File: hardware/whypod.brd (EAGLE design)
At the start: 100 x 80 mm, 13 parts, among them IC1 IC_USBLC6-2, X2 USB-A-S, Y1 CRYSTAL-GROUNDEDSMD-5X3.2

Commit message: Hardware updates
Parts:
- removed R3: 0R, rcl:R0603
- added C6, C7, C8, C9: (no value), rcl:C0603
- moved C4 2.80 mm to (56.1, 46.9)
- moved C1 2.54 mm to (25.4, 39.8)
- moved C2 2.54 mm to (25.4, 41.9)
- moved C3 2.54 mm to (51.0, 28.6)
- moved C5 2.54 mm to (51.5, 30.6)
- moved IC1 2.54 mm to (80.6, 44.4)
- moved R5 2.54 mm to (58.7, 36.7)
- moved U$2 2.54 mm to (44.2, 40.6)
- moved X2 2.54 mm to (89.3, 44.4)
- moved Y1 2.54 mm to (30.2, 40.9)
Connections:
- removed net N$5: R3.1, U$2.PD7
- new net LCD_BACKLIGHT: U$2.PC6
- new net SDIO_CLK: U$2.PC12
- new net SDIO_CMD: U$2.PD2
- new net SDIO_D0: U$2.PC8
- new net SDIO_D1: U$2.PC9
- new net SDIO_D2: U$2.PC10
- new net SDIO_D3: U$2.PC11
- net 3V: now also C6.1, C7.1, C8.1, C9.1
- net GND: now also C6.2, C7.2, C8.2, C9.2
- net LCD_CS: now also U$2.PD7; no longer R3.2
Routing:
- net 3V: track 2.42 -> 56.9 mm
- net DB2: track 4.29 -> 52.5 mm
- net SDIO_D1: track 0.00 -> 36.2 mm, vias 0 -> 1
- net SDIO_D0: track 0.00 -> 35.0 mm, vias 0 -> 1
- net LCD_BACKLIGHT: track 0.00 -> 34.4 mm
- net LCD_RD: track 15.2 -> 41.5 mm
- net LCD_WR: track 13.4 -> 39.4 mm
- net GND: track 0.00 -> 14.0 mm, vias 5 -> 8
- net LCD_CS: track 39.1 -> 49.4 mm
- net DB3: track 53.8 -> 45.9 mm
- net N$7: track 0.00 -> 4.28 mm
- net DB1: track 100.5 -> 97.9 mm
- net SD_CLK: track 64.8 -> 62.2 mm
- net T_CLK: track 46.7 -> 44.2 mm
- net SD_DO: track 62.7 -> 60.2 mm
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
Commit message: Hardware updated
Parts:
- added C10: (no value), rcl:C0603
- added JP1: (no value), pinhead-2:1X04SMD/90
- added R1, R2: 0R, rcl:R0603
- added R10, R11, R3, R6, R8: (no value), rcl:R0603
- added R7, R9: (no value), rcl:R0402
- added U1: USD-SOCKETUSD, SparkFun-Connectors:USD-SOCKET-PP
- moved IC1 27.9 mm to (52.7, 44.4)
- moved X2 27.9 mm to (61.4, 44.4)
- moved C3 14.6 mm to (36.4, 28.6)
- moved C4 14.6 mm to (41.5, 46.9)
- moved C8 14.6 mm to (22.4, 50.2)
- moved C9 14.6 mm to (38.9, 47.9)
- moved C6 14.6 mm to (23.4, 30.6)
- moved C7 14.6 mm to (19.1, 42.9)
- moved JP2 14.6 mm to (14.6, 15.2)
- moved U$2 14.6 mm to (29.6, 40.6)
- moved C1 14.6 mm to (10.8, 39.8)
- moved C2 14.6 mm to (10.8, 41.9)
- moved Y1 14.6 mm to (15.6, 40.9)
- moved C5 14.6 mm to (36.9, 30.6)
- moved R4 14.6 mm to (37.2, 20.7)
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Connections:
- new net N$5: R1.2, U$2.PC10
- new net N$8: R2.2, U$2.PC11
- new net SDIO_CD: R10.1, U$2.PD3, U1.CD1
- net 3V: now also C10.1, R10.2, R11.2, R3.2, R6.2, R7.2, R8.2, R9.2, U1.4
- net GND: now also C10.2, U1.6, U1.CD2, U1.GND1, U1.GND2
- net SDIO_CLK: now also R9.1, U1.5
- net SDIO_CMD: now also R11.1, U1.3
- net SDIO_D0: now also R3.1, U1.7
- net SDIO_D1: now also R6.1, U1.8
- net SDIO_D2: now also R1.1, R7.1, U1.1; no longer U$2.PC10
- net SDIO_D3: now also R2.1, R8.1, U1.2; no longer U$2.PC11
- net SWD_CLK: now also JP1.4
- net SWD_IO: now also JP1.3
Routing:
- net SDIO_CD: track 0.00 -> 42.5 mm
- net SWD_IO: track 0.00 -> 38.5 mm
- net 3V: track 56.9 -> 92.2 mm, vias 0 -> 3
- net SDIO_CMD: track 0.00 -> 31.6 mm
- net SWD_CLK: track 0.00 -> 28.6 mm
- net SDIO_D1: track 36.2 -> 64.5 mm, vias 1 -> 2
- net SDIO_D0: track 35.0 -> 63.1 mm, vias 1 -> 2
- net LCD_CS: track 49.4 -> 76.9 mm, vias 1 -> 2
- net SDIO_CLK: track 0.00 -> 26.6 mm
- net LCD_WR: track 39.4 -> 62.9 mm, vias 1 -> 2
- net N$5: track 0.00 -> 21.2 mm
- net N$8: track 0.00 -> 18.1 mm
- net SDIO_D3: track 0.00 -> 15.1 mm
- net DB3: track 45.9 -> 60.4 mm, vias 3 -> 2
- net LCD_RD: track 41.5 -> 55.3 mm
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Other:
- board size 100 x 80 mm -> 72.1 x 85.1 mm

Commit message: PCB updates
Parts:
- removed JP1: (no value), pinhead-2:1X04SMD/90
- added J1: AUDIO_JACK_TRRSSMD_RA, SparkFun-Connectors:AUDIO_JACK_3.5MM_TRRS_SMD_RA
- added JP3: (no value), pinhead-2:1X06SMD/90
- added U$1: WM8731, microdecv1:28-SSOP
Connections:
- new net AGND: U$1.P$15
- new net AVDD: U$1.P$14
- new net DBVDD: U$1.P$1
- new net DCVDD: U$1.P$27
- new net DGND: U$1.P$28
- new net HPGND: U$1.P$11
- new net HPVDD: U$1.P$8
- new net NRST: JP3.5, U$2.NRST
- new net SWD_SWO: JP3.6
- net 3V: now also JP3.1
- net GND: now also JP3.3
- net SWD_CLK: now also JP3.2; no longer JP1.4
- net SWD_IO: now also JP3.4; no longer JP1.3
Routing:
- net SWD_CLK: track 28.6 -> 7.10 mm
- net SWD_IO: track 38.5 -> 31.0 mm
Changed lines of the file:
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@@
 <element name="R10" library="rcl" package="R0603" value="" x="34.1685875" y="64.2112"/>
 <element name="R11" library="rcl" package="R0603" value="" x="35.867340625" y="66.1924" rot="R180"/>
-<element name="JP1" library="pinhead-2" package="1X04SMD/90" value="" x="64.77" y="62.865" rot="R270"/>
+<element name="JP3" library="pinhead-2" package="1X06SMD/90" value="" x="63.5" y="68.58" rot="R270"/>
+<element name="J1" library="SparkFun-Connectors" package="AUDIO_JACK_3.5MM_TRRS_SMD_RA" value="AUDIO_JACK_TRRSSMD_RA" x="19.05" y="83.82" rot="R270">
+<attribute name="PROD_ID" value="CONN-10676" x="19.05" y="83.82" size="1.778" layer="27" rot="R270" display="off"/>
+<attribute name="SF_ID" value="PRT-12639" x="19.05" y="83.82" size="1.778" layer="27" rot="R270" display="off"/>
+</element>
+<element name="U$1" library="microdecv1" package="28-SSOP" value="WM8731" x="19.05" y="63.5" rot="R270"/>
 </elements>
 <signals>
@@
 <via x="44.6786" y="66.3956" extent="1-16" drill="0.6" diameter="1.4224" shape="octagon"/>
 <wire x1="21.8918" y1="37.1146" x2="20.32" y2="37.1146" width="0.3048" layer="1"/>
+<contactref element="JP3" pad="3"/>
 </signal>
 <signal name="DB0">
@@
 <signal name="SWD_IO">
 <contactref element="U$2" pad="PA13"/>
-<contactref element="JP1" pad="3"/>
 <wire x1="37.3918" y1="45.1146" x2="42.3714" y2="45.1146" width="0.3048" layer="1"/>
 <wire x1="42.3714" y1="45.1146" x2="43.1038" y2="45.847" width="0.3048" layer="1"/>
-<wire x1="43.1038" y1="45.847" x2="43.1038" y2="54.5084" width="0.3048" layer="1"/>
-<wire x1="43.1038" y1="54.5084" x2="44.1452" y2="55.5498" width="0.3048" layer="1"/>
-<wire x1="61.0362" y1="55.5498" x2="44.1452" y2="55.5498" width="0.3048" layer="1"/>
-<wire x1="59.69" y1="59.055" x2="61.087" y2="59.055" width="0.3048" layer="1"/>
-<wire x1="61.0362" y1="55.5498" x2="61.7474" y2="56.261" width="0.3048" layer="1"/>
-<wire x1="61.7474" y1="56.261" x2="61.7474" y2="58.3946" width="0.3048" layer="1"/>
-<wire x1="61.7474" y1="58.3946" x2="61.087" y2="59.055" width="0.3048" layer="1"/>
+<wire x1="43.1038" y1="45.847" x2="43.1038" y2="50.6984" width="0.3048" layer="1"/>
+<contactref element="JP3" pad="4"/>
+<wire x1="58.42" y1="62.23" x2="54.6354" y2="62.23" width="0.3048" layer="1"/>
+<wire x1="54.6354" y1="62.23" x2="43.1038" y2="50.6984" width="0.3048" layer="1"/>
 </signal>
 <signal name="SWD_CLK">
 <contactref element="U$2" pad="PA14"/>
-<contactref element="JP1" pad="4"/>
-<wire x1="59.69" y1="56.515" x2="41.783" y2="56.515" width="0.3048" layer="1"/>
-<wire x1="41.783" y1="56.515" x2="35.6418" y2="50.3738" width="0.3048" layer="1"/>
+<wire x1="39.243" y1="53.975" x2="35.6418" y2="50.3738" width="0.3048" layer="1"/>
 <wire x1="35.6418" y1="48.3646" x2="35.6418" y2="50.3738" width="0.3048" layer="1"/>
+<contactref element="JP3" pad="2"/>
+<wire x1="39.243" y1="53.975" x2="58.42" y2="67.31" width="0" layer="19" extent="1-1"/>
 </signal>
 <signal name="N$6">
@@
 <wire x1="35.0185875" y1="64.2112" x2="35.013" y2="64.2112" width="0.6096" layer="1"/>
 <wire x1="35.013" y1="64.2112" x2="34.8234" y2="64.4008" width="0.6096" layer="1"/>
+<contactref element="JP3" pad="1"/>
+<wire x1="51.2182" y1="68.1482" x2="58.42" y2="69.85" width="0" layer="19" extent="1-1"/>
 <wire x1="38.9128" y1="47.012490625" x2="35.0185875" y2="64.2112" width="0" layer="19" extent="1-1"/>
 </signal>
@@
 <wire x1="43.9538" y1="60.413" x2="34.1418" y2="50.601" width="0.3048" layer="1"/>
 </signal>
+<signal name="NRST">
+<contactref element="JP3" pad="5"/>
+<contactref element="U$2" pad="NRST"/>
+<wire x1="21.8918" y1="40.1146" x2="58.42" y2="59.69" width="0" layer="19" extent="1-1"/>
+</signal>
+<signal name="SWD_SWO">
+<contactref element="JP3" pad="6"/>
+</signal>
+<signal name="DBVDD">
+<contactref element="U$1" pad="P$1"/>
+</signal>
+<signal name="HPGND">
+<contactref element="U$1" pad="P$11"/>
+</signal>
+<signal name="AVDD">
+<contactref element="U$1" pad="P$14"/>
+</signal>
+<signal name="DCVDD">
+<contactref element="U$1" pad="P$27"/>
+</signal>
+<signal name="DGND">
+<contactref element="U$1" pad="P$28"/>
+</signal>
+<signal name="AGND">
+<contactref element="U$1" pad="P$15"/>
+</signal>
+<signal name="HPVDD">
+<contactref element="U$1" pad="P$8"/>
+</signal>
 </signals>

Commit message: PCB updates
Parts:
- moved C10 22.2 mm to (53.3, 87.8)
- moved R6 22.2 mm to (58.6, 82.1)
- moved U1 22.2 mm to (52.0, 104.7)
- moved R3 22.2 mm to (58.6, 83.9)
- moved R8 22.2 mm to (47.4, 87.8)
- moved R2 22.2 mm to (53.3, 82.1)
- moved R1 22.2 mm to (53.3, 84.0)
- moved R11 22.2 mm to (46.0, 85.9)
- moved R9 22.2 mm to (52.6, 86.0)
- moved R10 22.2 mm to (44.3, 83.9)
- moved R7 22.2 mm to (50.2, 86.0)
- moved J1 21.9 mm to (25.4, 104.8)
- moved U$1 19.5 mm to (25.4, 81.9)
- moved IC1 1.91 mm to (50.8, 44.4)
- moved X2 1.91 mm to (59.5, 44.4)
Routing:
- net SDIO_CMD: track 31.6 -> 57.5 mm
- net SDIO_CD: track 42.5 -> 68.3 mm
- net SDIO_D1: track 64.5 -> 88.4 mm
- net SDIO_CLK: track 26.6 -> 50.5 mm
- net N$8: track 18.1 -> 42.0 mm
- net SDIO_D0: track 63.1 -> 87.0 mm
- net N$5: track 21.2 -> 45.1 mm
- net SWD_CLK: track 7.10 -> 2.61 mm
- net USB_D_P: track 15.6 -> 13.7 mm
- net USB_D_N: track 15.6 -> 13.7 mm
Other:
- board size 72.1 x 85.1 mm -> 65.1 x 104.8 mm

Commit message: PCB updated
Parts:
- removed JP3: (no value), pinhead-2:1X06SMD/90
- added JP1: (no value), pinhead-2:1X06SMD/90
- moved J1 7.62 mm to (17.8, 104.8)
- moved U$1 1.27 mm to (25.4, 83.2), turned to 90 degrees
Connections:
- removed net DGND: U$1.P$28
- new net I2C1_SCL: U$1.P$24, U$2.PB6
- new net I2C1_SDA: U$1.P$23, U$2.PB7
- new net I2S_WS: U$2.PA15
- net 3V: now also JP1.1; no longer JP3.1
- net AGND: now also J1.EARTH
- net GND: now also JP1.3, U$1.P$28; no longer JP3.3
- net NRST: now also JP1.5; no longer JP3.5
- net SWD_CLK: now also JP1.2; no longer JP3.2
- net SWD_IO: now also JP1.4; no longer JP3.4
- net SWD_SWO: now also JP1.6; no longer JP3.6
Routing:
- net SWD_CLK: track 2.61 -> 33.8 mm
- net I2S_WS: track 0.00 -> 13.2 mm, vias 0 -> 2
- net 3V: track 92.2 -> 102.4 mm
- net SWD_IO: track 31.0 -> 33.8 mm
- net LCD_CS: track 76.9 -> 78.2 mm
- net DB2: track 63.8 -> 65.1 mm
- net LCD_WR: track 62.9 -> 64.2 mm
- net DB3: track 60.4 -> 61.6 mm
- net LCD_RD: track 55.3 -> 56.6 mm
- net GND: vias 10 -> 11
- added copper zone on layer 1, net AGND

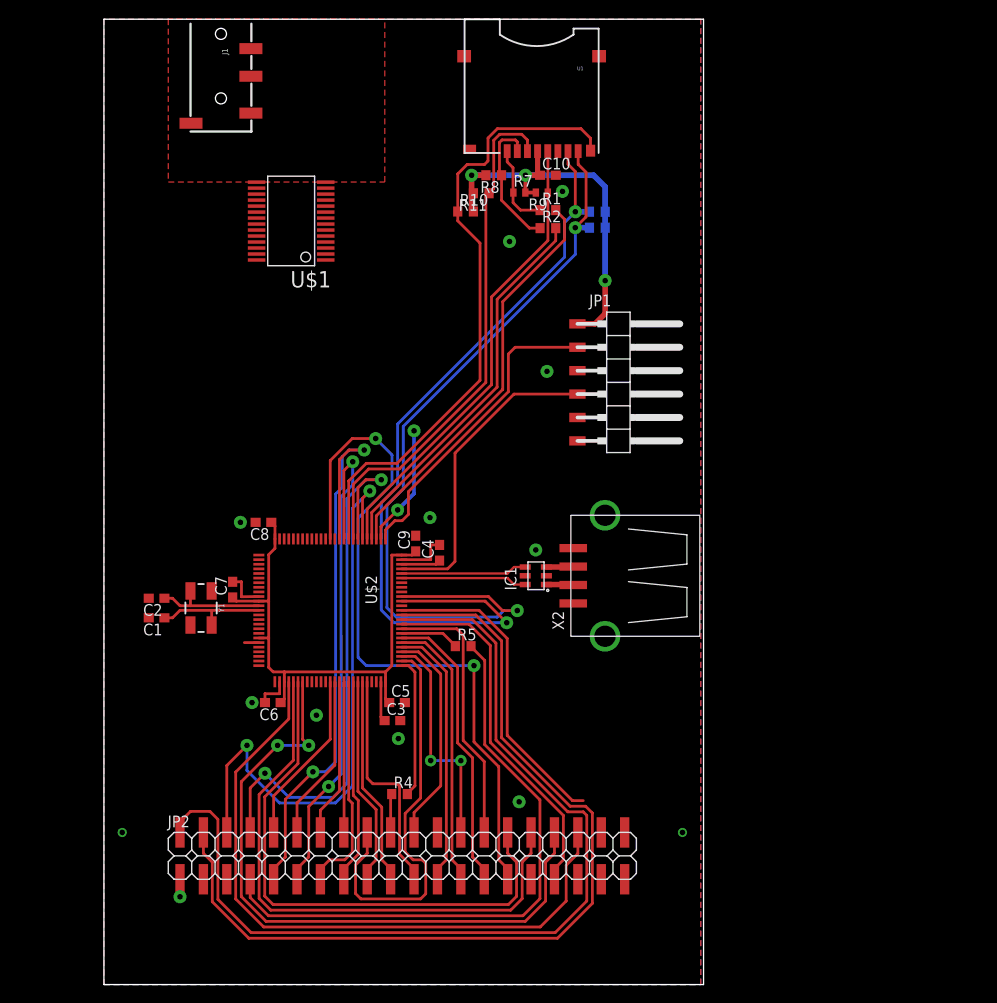
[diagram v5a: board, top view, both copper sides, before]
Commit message: DAC added
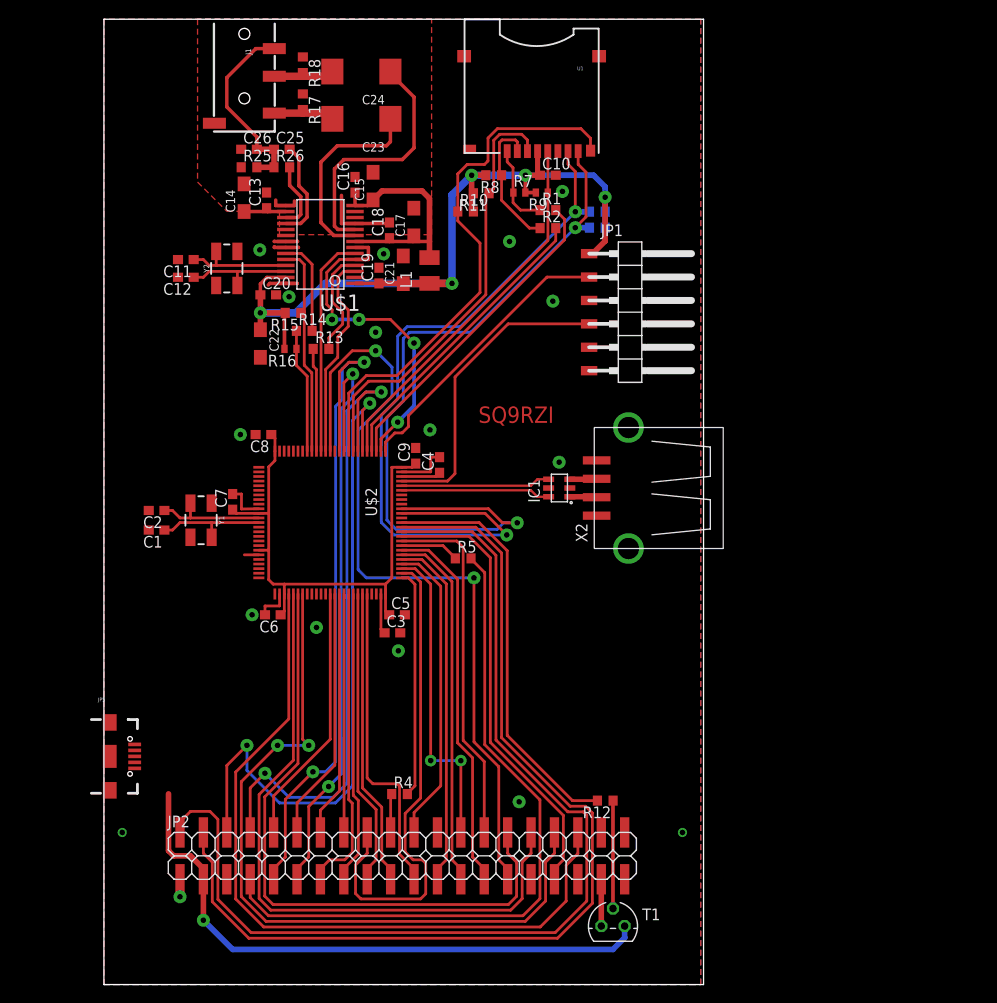
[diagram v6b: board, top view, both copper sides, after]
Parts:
- added C11, C12: 22 pF, rcl:C0603
- added C13, C16, C18, C19, C20: (no value), rcl:C0603
- added C14, C15, C17, C21, C22: (no value), rcl:SMC_A
- added C23, C24: (no value), rcl:SMC_E
- added C25: 1u, rcl:C0603
- added C26: 220p, rcl:C0603
- added JP5: USB_MICROB_PLUGCONN-11752, SparkFun-Connectors:USB-B-MICRO-SMD_V03
- added L1: (no value), rcl:L3225M
- added R12, R15: (no value), rcl:R0603
- added R13, R14: 0R, rcl:R0603
- added R16: (no value), rcl:R0402
- added R17, R18, R25: 47k, rcl:R0603
- added R26: 680, rcl:R0603
- added T1: BC557, transistor-pnp:TO92
- added Y2: CRYSTAL-GROUNDEDSMD-5X3.2, SparkFun-Clocks:CRYSTAL-SMD-5X3.2-4PAD
- moved IC1 9.86 mm to (53.3, 53.9)
- moved X2 9.86 mm to (62.0, 53.9)
- moved C7 9.53 mm to (19.1, 52.4)
- moved C1 9.52 mm to (10.8, 49.3)
- moved C2 9.52 mm to (10.8, 51.5)
- moved C3 9.52 mm to (36.4, 38.2)
- moved C4 9.52 mm to (41.5, 56.4)
- moved C5 9.52 mm to (36.9, 40.1)
- moved C6 9.52 mm to (23.4, 40.1)
- moved C8 9.52 mm to (22.4, 59.7)
- moved C9 9.52 mm to (38.9, 57.4)
- moved R5 9.52 mm to (44.1, 46.3)
- moved U$2 9.52 mm to (29.6, 50.1)
- moved Y1 9.52 mm to (15.6, 50.4)
- moved JP1 7.73 mm to (62.8, 78.1)
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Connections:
- removed net AVDD: U$1.P$14
- removed net DBVDD: U$1.P$1
- removed net DCVDD: U$1.P$27
- removed net HPGND: U$1.P$11
- removed net HPVDD: U$1.P$8
- removed net VCC: JP2.3
- new net A_3V: C15.+, C16.1, C17.+, C18.1, L1.2, U$1.P$14, U$1.P$8
- new net I2S_CK: U$1.P$3, U$2.PB3
- new net I2S_EXT_SD: U$1.P$6, U$2.PB4
- new net I2S_SD: R13.2, U$1.P$4
- new net LOUT: C23.+, U$1.P$9
- new net MICBIAS: R26.2, U$1.P$17
- new net MICIN: C25.2, U$1.P$18
- new net N$11: R12.1, T1.2
- new net N$12: C13.1, C14.+, U$1.P$16
- new net N$13: C23.-, J1.TIP, R17.2
- new net N$14: R13.1, U$2.PB5
- new net N$15: C24.-, J1.RING1, R18.2
- new net N$16: R14.1, R16.1, U$2.PB7
- new net N$55: C25.1, C26.2, J1.RING2, R25.2, R26.1
- new net ROUT: C24.+, U$1.P$10
- new net XTI: C11.1, U$1.P$25, Y2.3
- new net XTO: C12.1, U$1.P$26, Y2.1
- net 3V: now also C19.1, C20.1, C21.+, C22.+, JP2.3, L1.1, R15.2, R16.2, T1.1, U$1.P$1, U$1.P$27
- net AGND: now also C13.2, C14.-, C15.-, C16.2, C17.-, C18.2, C26.1, R17.1, R18.1, R25.1, U$1.P$11
- net GND: now also C11.2, C12.2, C19.2, C20.2, C21.-, C22.-, JP5.GND1, U$1.P$21, U$1.P$22, Y2.2, Y2.4
- net I2C1_SCL: now also R15.1
- net I2C1_SDA: now also R14.2; no longer U$2.PB7
- net I2S_WS: now also U$1.P$5, U$1.P$7
- net LCD_BACKLIGHT: now also R12.2
- net LED_A: now also T1.3
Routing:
- net 3V: track 102.4 -> 221.8 mm, vias 3 -> 6
- net ROUT: track 0.00 -> 27.5 mm
- net A_3V: track 0.00 -> 26.0 mm
- net I2S_EXT_SD: track 0.00 -> 24.1 mm
- net I2C1_SCL: track 0.00 -> 23.3 mm
- net I2S_WS: track 13.2 -> 36.4 mm, vias 2 -> 5
- net I2S_CK: track 0.00 -> 22.5 mm
- net LOUT: track 0.00 -> 21.8 mm
- net N$55: track 0.00 -> 21.3 mm
- net N$16: track 0.00 -> 13.8 mm
- net I2S_SD: track 0.00 -> 12.0 mm
- net XTI: track 0.00 -> 11.8 mm
- net XTO: track 0.00 -> 11.8 mm
- net N$11: track 0.00 -> 11.7 mm
- net AGND: track 0.00 -> 11.4 mm
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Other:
- board text added: "SQ9RZI"

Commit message: Minor updates
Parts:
- added C27, C28: (no value), rcl:C0603
- added F3: 1206L012, polyfuse-smd_10:1206L
- added LED1: (no value), led:CHIP-LED0603
- added R19, R20: (no value), rcl:R0603
- added U$3: MCP73831SOT-23-5, lion-charger:SOT-23-5
- T1: value BC557 -> (none); device transistor-pnp:TO92 -> transistor:SOT23-BEC
- moved T1 5.32 mm to (55.1, 5.51), flipped to the bottom, turned to 270 degrees
- moved C10 5.08 mm to (48.2, 87.8)
- moved IC1 5.08 mm to (48.3, 53.9)
- moved R1 5.08 mm to (48.2, 84.0)
- moved R12 5.08 mm to (54.4, 20.0)
- moved R2 5.08 mm to (48.2, 82.1)
- moved R4 5.08 mm to (32.1, 20.7)
- moved R5 5.08 mm to (39.0, 46.3)
- moved U1 5.08 mm to (47.0, 104.7)
- moved C13 5.08 mm to (17.7, 85.1)
- moved C22 5.08 mm to (17.0, 69.6)
- moved C23 5.08 mm to (27.9, 94.0)
- moved C24 5.08 mm to (27.9, 99.1)
- moved C25 5.08 mm to (19.3, 90.7)
- moved C6 5.08 mm to (18.3, 40.1)
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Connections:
- new net N$17: R19.1, U$3.5
- new net N$18: R20.2, U$3.1
- new net N$19: LED1.C, R20.1
- new net N$20: F3.2, JP5.VBUS1
- new net VBAT: C27.1, U$3.3
- new net VBUS: C28.1, F3.1, LED1.A, U$3.4
- net 3V: now also T1.E; no longer T1.1
- net GND: now also C27.2, C28.2, R19.2, U$3.2
- net LED_A: now also T1.C; no longer T1.3
- net N$11: now also T1.B; no longer T1.2
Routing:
- net VBUS: track 0.00 -> 3.84 mm
- net N$20: track 0.00 -> 2.33 mm
- net N$11: track 11.7 -> 13.9 mm, vias 0 -> 1
- net GND: track 24.1 -> 26.2 mm, vias 15 -> 16
- net VBAT: track 0.00 -> 1.78 mm
- net N$18: track 0.00 -> 1.52 mm
- net N$17: track 0.00 -> 1.31 mm
- net 3V: track 221.8 -> 220.5 mm
- net LED_A: track 5.08 -> 5.92 mm, vias 0 -> 1

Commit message: PCB updated
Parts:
- added C29: (no value), rcl:C0603
- added C30: (no value), rcl:SMC_E
- added U$4: EVQWK, mw:EVQWK
- added U$5: TPS2500, mw:DRC10
- moved C22 4.72 mm to (13.6, 72.9), turned to 180 degrees
- moved F3 1.91 mm to (3.76, 27.5)
- moved R19 1.91 mm to (5.66, 28.8)
- moved R20 1.91 mm to (4.83, 34.8)
- moved U$3 1.91 mm to (4.72, 32.1)
- moved C27 1.91 mm to (1.14, 33.3)
- moved C28 1.91 mm to (1.14, 30.9)
- moved JP5 1.91 mm to (-1.27, 24.8)
- moved LED1 1.91 mm to (1.75, 34.8)
- moved JP1 1.73 mm to (59.5, 78.1)
- moved IC1 0.64 mm to (48.9, 53.9)
- moved X2 0.63 mm to (57.6, 53.9)
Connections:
- new net ENUSB: U$2.PC7, U$5.7
- new net N$22: U$5.10
- new net N$23: U$5.3, U$5.4
- new net USBFAULT: U$2.PA8, U$5.8
- net GND: now also C29.2, C30.-, U$4.COM, U$4.GND, U$4.SW1@1, U$4.SW1@2, U$5.2, U$5.5, U$5.T
- net _5V: now also C29.1, C30.+, U$5.9
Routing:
- net USBFAULT: track 0.00 -> 21.8 mm
- net ENUSB: track 0.00 -> 19.4 mm
- net _5V: track 0.00 -> 7.96 mm
- net GND: track 26.2 -> 33.8 mm
- net SWD_CLK: track 31.2 -> 32.9 mm
- net SWD_IO: track 33.6 -> 35.3 mm
- net SDIO_D0: track 80.8 -> 82.5 mm
- net 3V: track 220.5 -> 219.6 mm
- net USB_D_N: track 16.2 -> 16.9 mm
- net USB_D_P: track 16.2 -> 16.9 mm
- net SDIO_D1: track 82.8 -> 82.2 mm
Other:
- board size 65.1 x 104.8 mm -> 68.2 x 104.8 mm
